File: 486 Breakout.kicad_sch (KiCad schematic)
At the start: 36 parts, among them J1 PWR, J10 Conn_02x03_Counter_Clockwise, J11 Byte Enabled, J12 FPU, J13 Input, J14 Bus Size, J15 Bus Arbitration, J2 Conn_02x04_Counter_Clockwise, J3 Not Connected, J4 Address Bus, J5 Data Bus, J6 Conn_02x03_Counter_Clockwise, J7 Control Bus, J8 Cache, J9 Parity

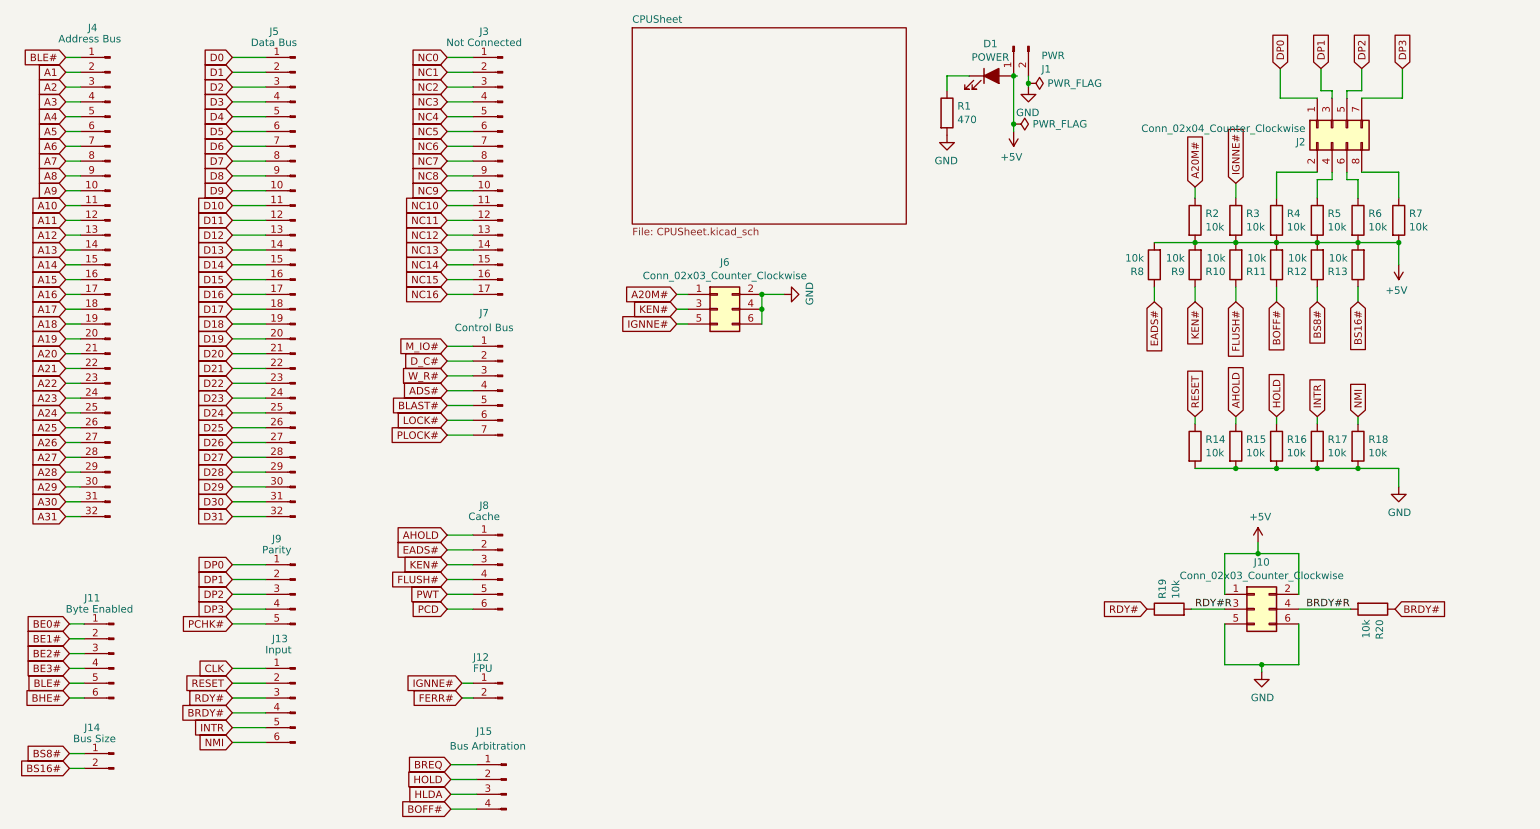
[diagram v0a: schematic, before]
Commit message: Updating the 486 Breakout Board
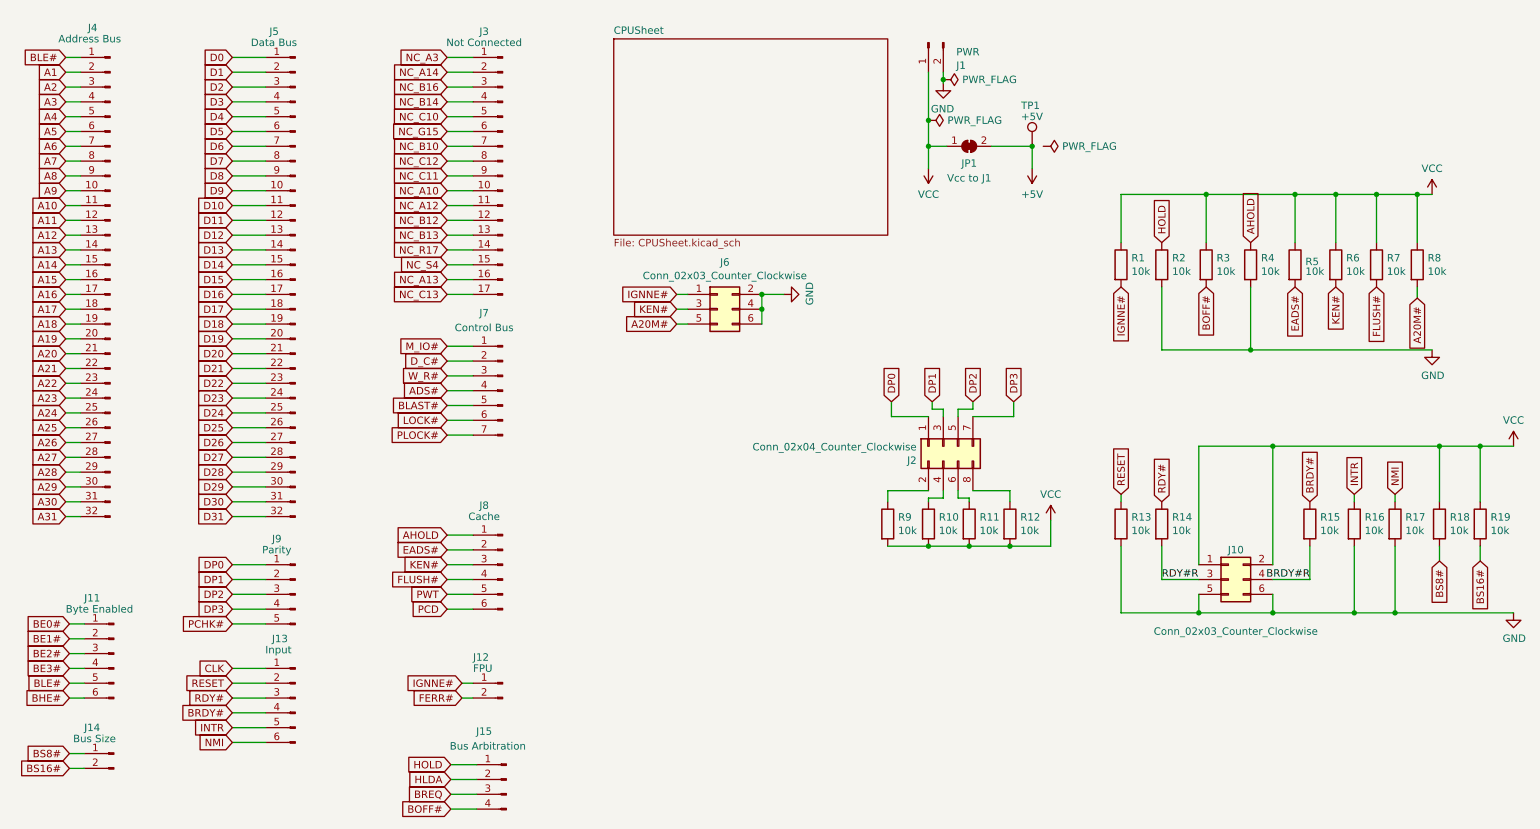
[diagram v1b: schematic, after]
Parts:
- removed D1: POWER, LED_THT:LED_D3.0mm, symbol Device:LED_ALT
- removed R1: 470, Resistor_THT:R_Axial_DIN0204_L3.6mm_D1.6mm_P7.62mm_Horizontal, symbol Device:R
- added JP1: Vcc to J1, Jumper:SolderJumper-2_P1.3mm_Bridged_Pad1.0x1.5mm, symbol Jumper:SolderJumper_2_Bridged
- added TP1: +5V, TestPoint:TestPoint_Pad_2.0x2.0mm, symbol Connector:TestPoint
- renumbered R3 to R1, R5 to R10, R6 to R11, R7 to R12, R14 to R13, R19 to R14, R20 to R15, R17 to R16, R18 to R17, R12 to R18, R13 to R19, R16 to R2, R11 to R3, R15 to R4, R8 to R5, R9 to R6, R10 to R7, R2 to R8, R4 to R9
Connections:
- net +5V: now also JP1.2 (B), TP1.1; no longer J1.1 (Pin_1), J10.1 (Pin_1), J10.2 (Pin_2), R1.2, R10.2, R11.2, R12.2, R18.2, R19.2, R3.2, R5.2, R6.2, R7.2, R8.2, R9.2
- net A20M#: now also J6.5 (Pin_5), R8.2; no longer J6.1 (Pin_1), R8.1
- net BOFF#: now also R3.2; no longer R3.1
- net BREQ: now also J15.3 (Pin_3); no longer J15.1 (Pin_1)
- net BS16#: now also R19.2; no longer R19.1
- net BS8#: now also R18.2; no longer R18.1
- net EADS#: now also R5.2; no longer R5.1
- net FLUSH#: now also R7.2; no longer R7.1
- net HLDA: now also J15.2 (Pin_2); no longer J15.3 (Pin_3)
- net HOLD: now also J15.1 (Pin_1); no longer J15.2 (Pin_2)
- net IGNNE#: now also J6.1 (Pin_1), R1.2; no longer J6.5 (Pin_5), R1.1
- net KEN#: now also R6.2; no longer R6.1
- net NC0 renamed NC_A3
- net NC1 renamed NC_A14
- net NC10 renamed NC_A12
- net NC11 renamed NC_B12
- net NC12 renamed NC_B13
- net NC13 renamed NC_R17
- net NC14 renamed NC_S4
- net NC15 renamed NC_A13
- net NC16 renamed NC_C13
- net NC2 renamed NC_B16
- net NC3 renamed NC_B14
- net NC4 renamed NC_C10
- net NC5 renamed NC_G15
- net NC6 renamed NC_B10
- net NC7 renamed NC_C12
- net NC8 renamed NC_C11
- net NC9 renamed NC_A10
- new net VCC: J1.1 (Pin_1), J10.1 (Pin_1), J10.2 (Pin_2), JP1.1 (A), R1.1, R10.2, R11.2, R12.2, R18.1, R19.1, R3.1, R5.1, R6.1, R7.1, R8.1, R9.2
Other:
- moved on the sheet: J1, J10, J2, R1, R10, R11, R12, R13, R14, R15, R16, R17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
